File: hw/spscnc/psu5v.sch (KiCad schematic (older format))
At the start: 30 parts, among them Q10 KIA50N06B, U21 LM2596, U9 LM2596

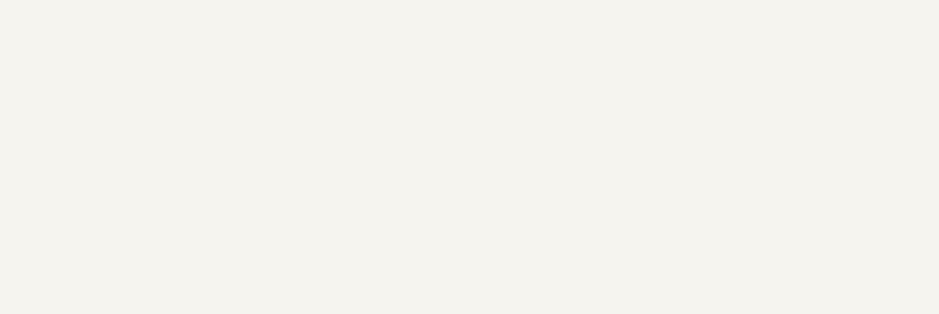
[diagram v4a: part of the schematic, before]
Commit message: Prototype corrections without new PCB
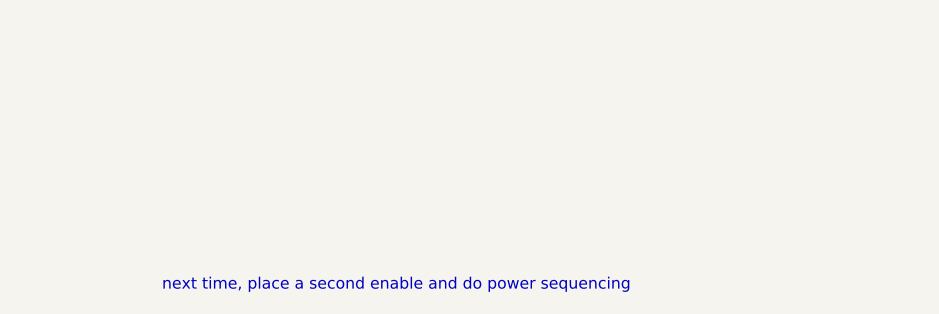
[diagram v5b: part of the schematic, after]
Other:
- note added: "next time, place a second enable and do power sequencing"
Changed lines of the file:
@@
 Wire Wire Line
 	7475 2950 8075 2950
+Text Notes 5250 8775 0    50   ~ 0
+next time, place a second enable and do power sequencing
 $EndSCHEMATC

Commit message: Revision 1.1.0 With only critical corrections. Pending some work on the relays as that part could be remade from scratch for flexibility.
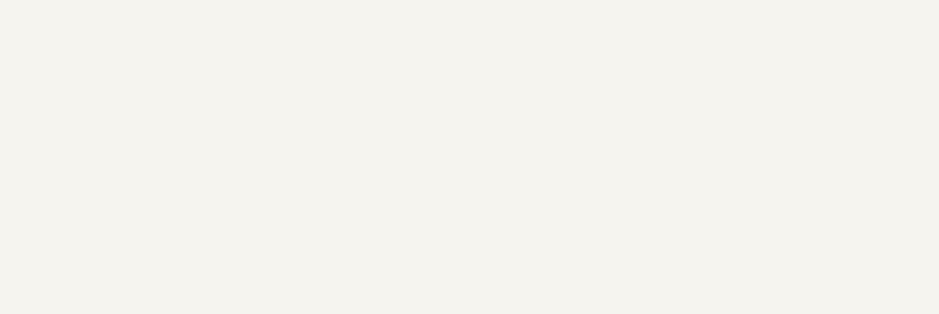
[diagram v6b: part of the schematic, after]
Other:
- note removed: "next time, place a second enable and do power sequencing"
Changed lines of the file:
@@
 Sheet 3 17
 Title "Trinamic FluidNC CNC Controller"
-Date "2022-02-12"
-Rev "1.0.1"
+Date "2022-04-29"
+Rev "1.1.0"
 Comp ""
 Comment1 ""
@@
 	1    0    0    -1
 $EndComp
-Wire Wire Line
-	4425 2550 5275 2550
 $Comp
 L power:GND-power #PWR034
@@
 Text Label 5900 5350 0    50   ~ 0
 ~ENABLE
-Text Label 6125 3375 2    50   ~ 0
-~ENABLE
 Wire Wire Line
 	5775 3800 6950 3800
-Wire Wire Line
-	6225 3375 6225 3250
-Wire Wire Line
-	6125 3375 6225 3375
 $Comp
 L Device:R_Small R?
@@
 Wire Wire Line
 	7475 2950 8075 2950
-Text Notes 5250 8775 0    50   ~ 0
-next time, place a second enable and do power sequencing
+Wire Wire Line
+	6225 3375 6225 3250
+Wire Wire Line
+	4425 2550 5275 2550
+Wire Wire Line
+	6125 3375 6225 3375
+Text Label 6125 3375 2    50   ~ 0
+~ENABLE
 $EndSCHEMATC
